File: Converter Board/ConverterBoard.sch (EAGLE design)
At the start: 40 parts

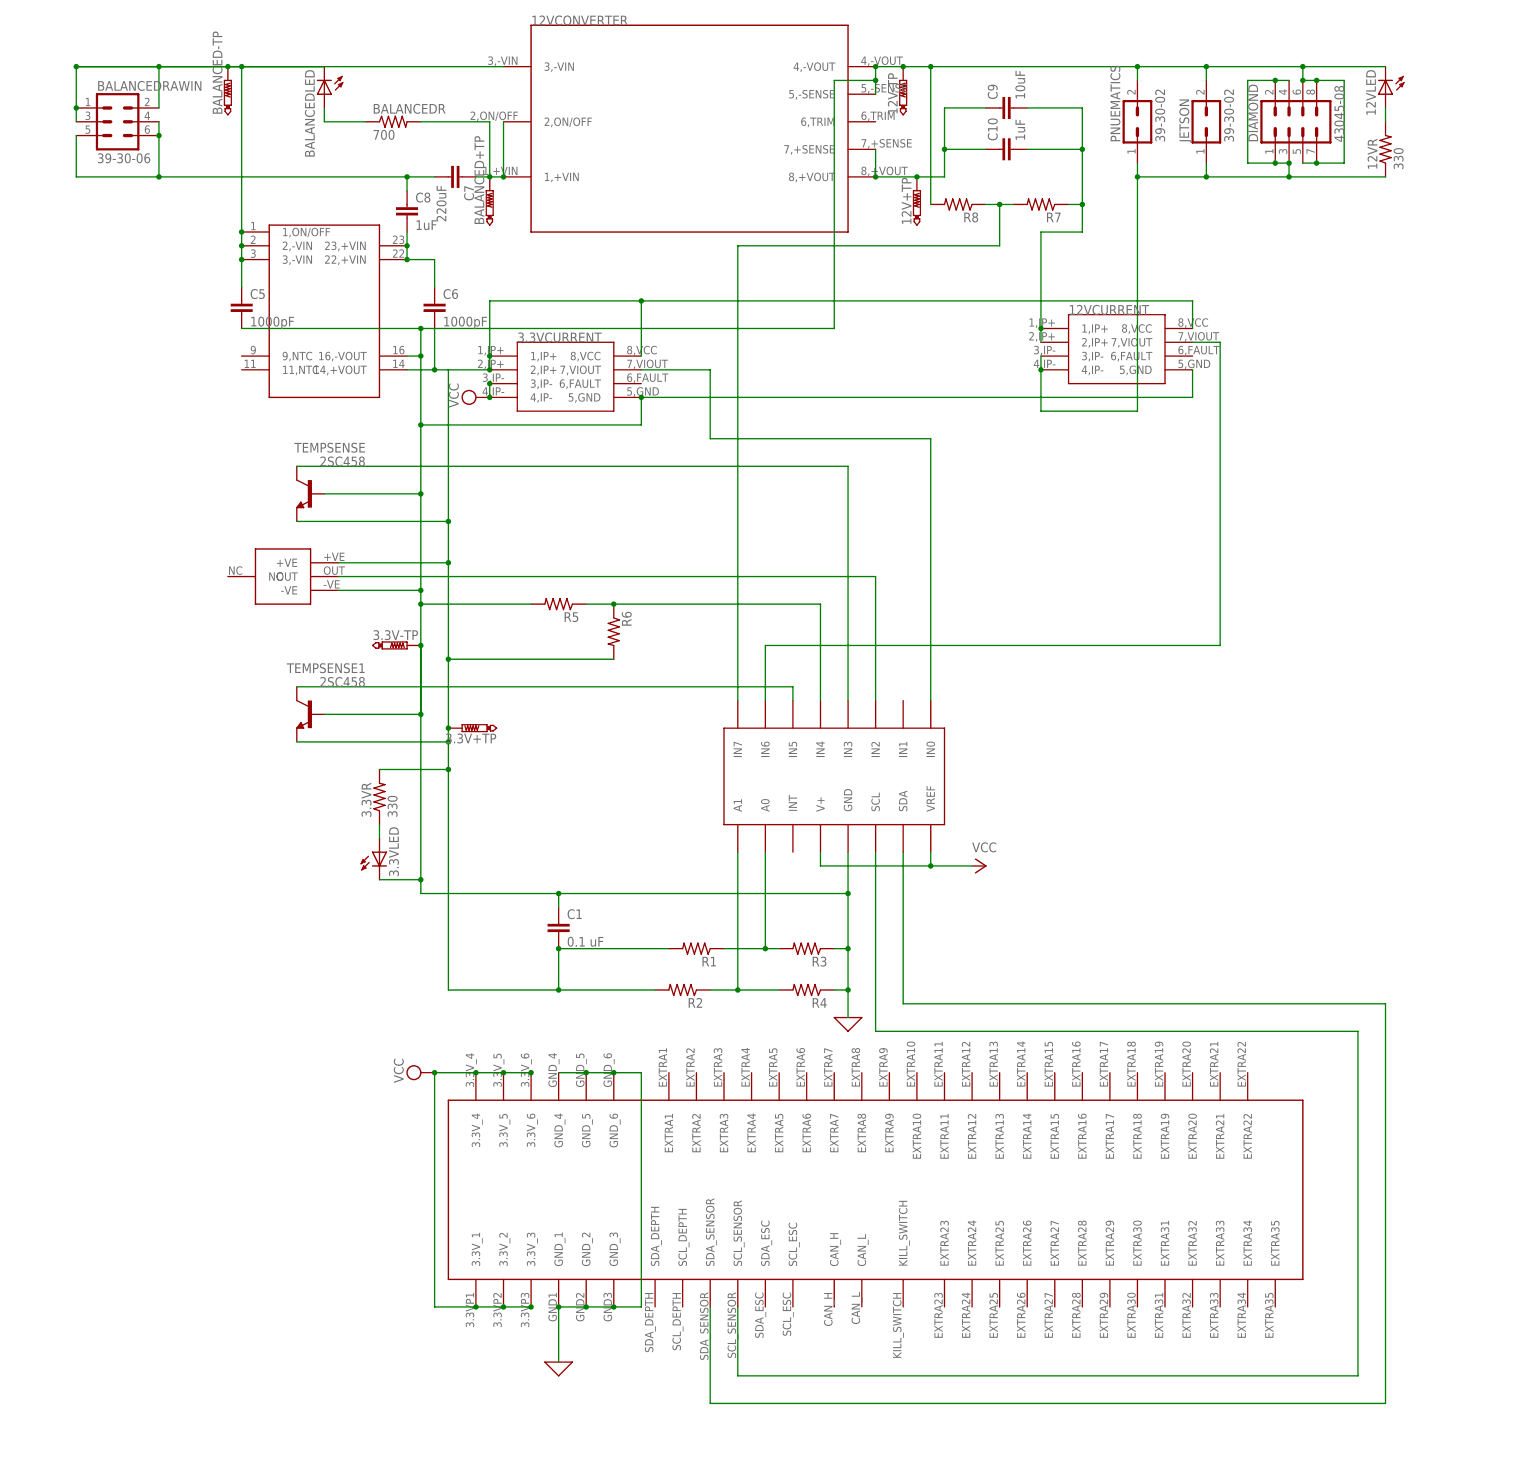
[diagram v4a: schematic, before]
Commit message: Finished Rev 3 of converter board
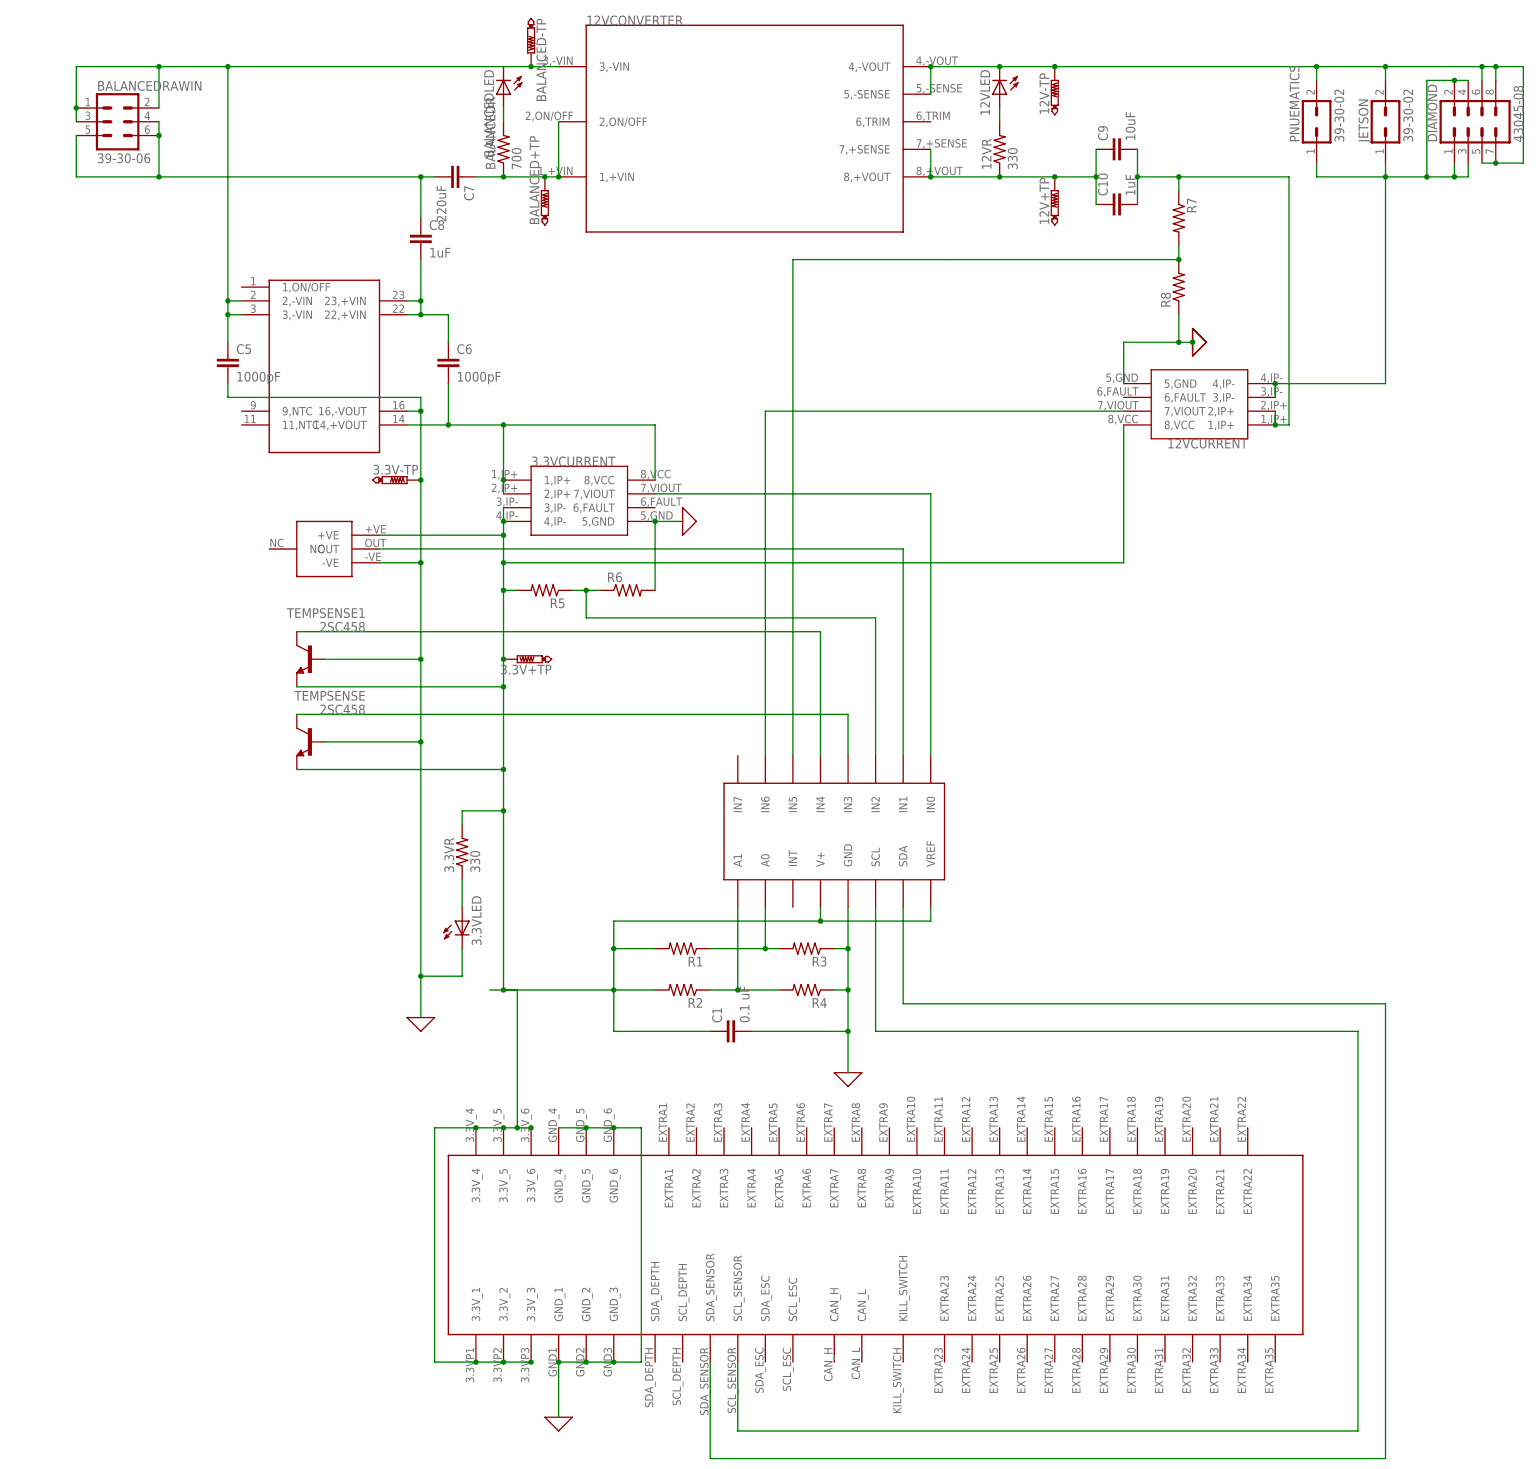
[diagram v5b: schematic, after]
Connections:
- net 12IDATA renamed 12VCURRENTDATA
- net 3.3IDATA renamed 3.3VCURRENTDATA
- net 3.3VC renamed 3.3VCONVIN
- removed net 12V+: 12V+TP.TP, 12VCONVERTER.7,+SENSE, 12VCONVERTER.8,+VOUT, C10.1, C9.1
- removed net 12VCIN: 12VCONVERTER.1,+VIN, 12VCONVERTER.2,ON/OFF, 12VCURRENT.1,IP+, 12VCURRENT.2,IP+, BALANCED+TP.TP, BALANCEDR.2, C10.2, C7.1, C9.2, R7.1
- removed net 12VCOUT: 12VCURRENT.3,IP-, 12VCURRENT.4,IP-, 12VR.1, DIAMOND.1, DIAMOND.2, DIAMOND.3, DIAMOND.4, JETSON.1, PNUEMATICS.1
- removed net 12VDATA: R7.2, R8.1, U$8.IN7
- removed net 3.3V+: 12VCURRENT.8,VCC, 3.3V+TP.TP, 3.3VCURRENT.1,IP+, 3.3VCURRENT.2,IP+, 3.3VCURRENT.8,VCC, 3.3VR.2, C1.2, C6.2, R1.2, R2.2, R6.2, TEMPSENSE.E, TEMPSENSE1.E, U$2.14,+VOUT, U$6.+VE
- removed net GND: 12V-TP.TP, 12VCONVERTER.4,-VOUT, 12VCONVERTER.5,-SENSE, 12VCURRENT.5,GND, 12VLED.C, 3.3V-TP.TP, 3.3VCURRENT.5,GND, 3.3VLED.C, C1.1, C5.2, DIAMOND.5, DIAMOND.6, DIAMOND.7, DIAMOND.8, JETSON.2, PNUEMATICS.2, R3.1, R4.1, R5.2, R8.2, TEMPSENSE.B, TEMPSENSE1.B, U$2.16,-VOUT, U$6.-VE, U$8.GND
- removed net VCC: 3.3VCURRENT.3,IP-, 3.3VCURRENT.4,IP-, U$3.3.3V_1, U$3.3.3V_2, U$3.3.3V_3, U$3.3.3V_4, U$3.3.3V_5, U$3.3.3V_6, U$8.V+, U$8.VREF
- new net 12VCONV+: 12V+TP.TP, 12VCONVERTER.7,+SENSE, 12VCONVERTER.8,+VOUT, 12VR.1, C10.1, C9.1
- new net 12VCONVIN: 12VCONVERTER.1,+VIN, 12VCONVERTER.2,ON/OFF, BALANCED+TP.TP, BALANCEDR.1, C7.1
- new net 12VCURRENTIN: 12VCURRENT.1,IP+, 12VCURRENT.2,IP+, C10.2, C9.2, R7.1
- new net 12VCURRENTOUT: 12VCURRENT.3,IP-, 12VCURRENT.4,IP-, DIAMOND.1, DIAMOND.2, DIAMOND.3, DIAMOND.4, JETSON.1, PNUEMATICS.1
- new net 12VDIV: R7.2, R8.2, U$8.IN5
- new net 3.3VCONVOUT: 3.3VCURRENT.1,IP+, 3.3VCURRENT.2,IP+, 3.3VCURRENT.8,VCC, C6.2, U$2.14,+VOUT
- new net 3.3VCURRENTOUT: 12VCURRENT.8,VCC, 3.3V+TP.TP, 3.3VCURRENT.3,IP-, 3.3VCURRENT.4,IP-, 3.3VR.2, C1.1, R1.2, R2.2, R5.2, TEMPSENSE.E, TEMPSENSE1.E, U$3.3.3V_1, U$3.3.3V_2, U$3.3.3V_3, U$3.3.3V_4, U$3.3.3V_5, U$3.3.3V_6, U$6.+VE, U$8.V+, U$8.VREF
- new net CMGND: 12V-TP.TP, 12VCONVERTER.4,-VOUT, 12VCONVERTER.5,-SENSE, 12VCURRENT.5,GND, 12VLED.C, 3.3V-TP.TP, 3.3VCURRENT.5,GND, 3.3VLED.C, C1.2, C5.2, DIAMOND.5, DIAMOND.6, DIAMOND.7, DIAMOND.8, JETSON.2, PNUEMATICS.2, R3.1, R4.1, R6.2, R8.1, TEMPSENSE.B, TEMPSENSE1.B, U$2.16,-VOUT, U$6.-VE, U$8.GND
- net 3.3VDATA: now also U$8.IN2; no longer U$8.IN4
- net BALANCEDGND: no longer U$2.1,ON/OFF
- net BALANCEDLED: now also BALANCEDR.2; no longer BALANCEDR.1
- net HUMIDITYDATA: now also U$8.IN1; no longer U$8.IN2
- net TEMP1DATA: now also U$8.IN4; no longer U$8.IN5
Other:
- moved on the sheet: 12V+TP, 12V-TP, 12VCONVERTER, 12VCURRENT, 12VLED, 12VR, 3.3V+TP, 3.3V-TP, 3.3VCURRENT, 3.3VLED, 3.3VR, BALANCED+TP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

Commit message: Finished rev3 of board, made gerber files
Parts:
- removed C1: 0.1 uF, resistor:C-EU025-024X044
- removed C10, C8: 1uF, resistor:C-EU025-024X044
- removed C6: 1000pF, resistor:C-EU025-024X044
- removed C7: 220uF, resistor:C-EU025-024X044
- removed C9: 10uF, resistor:C-EU025-024X044
- added C11, C14: 1uF, capacitor-wima:C5/3
- added C12: 220uF, capacitor-wima:C5/3
- added C13: 10uF, capacitor-wima:C5/3
- added C3, C4: 1000pF, capacitor-wima:C5/3
- added SCL, SDA: TPPAD1-20, testpad:TPPAD1-20
- C5: value 1000pF -> 0.1uF; device resistor:C-EU025-024X044 -> capacitor-wima:C2.5/2
- renumbered U$8 to ADC
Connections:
- removed net 3.3VGND: U$3.GND_1, U$3.GND_2, U$3.GND_3, U$3.GND_4, U$3.GND_5, U$3.GND_6
- net 12VCONV+: now also C13.1, C14.1; no longer C10.1, C9.1
- net 12VCONVIN: now also C12.2; no longer C7.1
- net 12VCURRENTIN: now also C13.2, C14.2; no longer C10.2, C9.2
- net 3.3VCONVIN: now also C11.2, C3.1; no longer C6.1, C8.2
- net 3.3VCONVOUT: now also C3.2; no longer C6.2
- net 3.3VCURRENTOUT: now also C5.2; no longer C1.1
- net BALANCED+: now also C11.1, C12.1; no longer C7.2, C8.1
- net BALANCEDGND: now also C4.1; no longer C5.1
- net CMGND: now also C4.2, C5.1, U$3.GND_1, U$3.GND_2, U$3.GND_3, U$3.GND_4, U$3.GND_5, U$3.GND_6; no longer C1.2, C5.2
- net SCL: now also SCL.TP
- net SDA: now also SDA.TP
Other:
- moved on the sheet: C5

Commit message: Revamped Converter Board
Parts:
- added 12V, 3.3V: 39-30-02, con-molex-mini-fit:39-30-02
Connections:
- removed net 12VCONVIN: 12VCONVERTER.1,+VIN, 12VCONVERTER.2,ON/OFF, BALANCED+TP.TP, BALANCEDR.1, C12.2
- removed net 12VCURRENTIN: 12VCURRENT.1,IP+, 12VCURRENT.2,IP+, C13.2, C14.2, R7.1
- net 12VCONV+: now also 12VCURRENT.1,IP+, 12VCURRENT.2,IP+, R7.1
- net 12VCURRENTOUT: now also 12V.1
- net 3.3VCURRENTOUT: now also 3.3V.1
- net BALANCED+: now also 12VCONVERTER.1,+VIN, 12VCONVERTER.2,ON/OFF, BALANCED+TP.TP, BALANCEDR.1
- net BALANCEDGND: now also C12.2
- net CMGND: now also 12V.2, 3.3V.2, C13.2, C14.2
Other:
- moved on the sheet: C12, C13, C14
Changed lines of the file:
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@@
 <?xml version="1.0" encoding="utf-8"?>
 <!DOCTYPE eagle SYSTEM "eagle.dtd">
-<eagle version="8.6.0">
+<eagle version="8.3.2">
 <drawing>
 <settings>
@@
 <part name="SDA" library="testpad" library_urn="urn:adsk.eagle:library:385" deviceset="TP" device="PAD1-20" package3d_urn="urn:adsk.eagle:package:27950/1"/>
 <part name="SCL" library="testpad" library_urn="urn:adsk.eagle:library:385" deviceset="TP" device="PAD1-20" package3d_urn="urn:adsk.eagle:package:27950/1"/>
+<part name="12V" library="con-molex-mini-fit" deviceset="39-30-?02?" device=""/>
+<part name="3.3V" library="con-molex-mini-fit" deviceset="39-30-?02?" device=""/>
 </parts>
 <sheets>
@@
 <instance part="C4" gate="G$1" x="-45.72" y="35.56"/>
 <instance part="C11" gate="G$1" x="-10.16" y="58.42"/>
-<instance part="C12" gate="G$1" x="-5.08" y="68.58" rot="R90"/>
-<instance part="C13" gate="G$1" x="116.84" y="73.66" rot="R90"/>
-<instance part="C14" gate="G$1" x="116.84" y="63.5" rot="R90"/>
+<instance part="C12" gate="G$1" x="-27.94" y="78.74" rot="R180"/>
+<instance part="C13" gate="G$1" x="124.46" y="78.74" rot="R180"/>
+<instance part="C14" gate="G$1" x="114.3" y="78.74" rot="R180"/>
 <instance part="C5" gate="G$1" x="48.26" y="-88.9" rot="R270"/>
 <instance part="SDA" gate="G$1" x="104.14" y="-81.28"/>
 <instance part="SCL" gate="G$1" x="124.46" y="-91.44" rot="R180"/>
+<instance part="12V" gate="G$1" x="144.78" y="78.74" rot="R90"/>
+<instance part="3.3V" gate="G$1" x="17.78" y="-93.98"/>
 </instances>
 <busses>
@@
 <pinref part="BALANCEDRAWIN" gate="G$1" pin="5"/>
 <wire x1="-73.66" y1="76.2" x2="-73.66" y2="68.58" width="0.1524" layer="91"/>
-<wire x1="-58.42" y1="68.58" x2="-10.16" y2="68.58" width="0.1524" layer="91"/>
+<wire x1="-58.42" y1="68.58" x2="-27.94" y2="68.58" width="0.1524" layer="91"/>
 <junction x="-58.42" y="68.58"/>
-<wire x1="-10.16" y1="68.58" x2="-7.62" y2="68.58" width="0.1524" layer="91"/>
+<wire x1="-27.94" y1="68.58" x2="-10.16" y2="68.58" width="0.1524" layer="91"/>
 <wire x1="-10.16" y1="60.96" x2="-10.16" y2="68.58" width="0.1524" layer="91"/>
+<pinref part="C11" gate="G$1" pin="1"/>
 <junction x="-10.16" y="68.58"/>
-<pinref part="C11" gate="G$1" pin="1"/>
+<pinref part="BALANCEDR" gate="G$1" pin="1"/>
+<pinref part="12VCONVERTER" gate="G$1" pin="1,+VIN"/>
+<wire x1="5.08" y1="68.58" x2="12.7" y2="68.58" width="0.1524" layer="91"/>
+<pinref part="12VCONVERTER" gate="G$1" pin="2,ON/OFF"/>
+<wire x1="12.7" y1="68.58" x2="15.24" y2="68.58" width="0.1524" layer="91"/>
+<wire x1="15.24" y1="78.74" x2="15.24" y2="68.58" width="0.1524" layer="91"/>
+<junction x="15.24" y="68.58"/>
+<pinref part="BALANCED+TP" gate="G$1" pin="TP"/>
+<junction x="12.7" y="68.58"/>
+<wire x1="-10.16" y1="68.58" x2="5.08" y2="68.58" width="0.1524" layer="91"/>
+<junction x="5.08" y="68.58"/>
 <pinref part="C12" gate="G$1" pin="1"/>
+<wire x1="-27.94" y1="76.2" x2="-27.94" y2="68.58" width="0.1524" layer="91"/>
+<junction x="-27.94" y="68.58"/>
 </segment>
 </net>
@@
 <wire x1="-7.62" y1="-106.68" x2="-7.62" y2="-149.86" width="0.1524" layer="91"/>
 <pinref part="U$3" gate="G$1" pin="3.3V_6"/>
-<junction x="10.16" y="-106.68"/>
 <pinref part="U$3" gate="G$1" pin="3.3V_5"/>
 <junction x="5.08" y="-106.68"/>
@@
 <pinref part="C5" gate="G$1" pin="2"/>
 <junction x="43.18" y="-88.9"/>
+<pinref part="3.3V" gate="G$1" pin="1"/>
+<wire x1="10.16" y1="-93.98" x2="10.16" y2="-106.68" width="0.1524" layer="91"/>
+<junction x="10.16" y="-106.68"/>
 </segment>
 </net>
@@
 <wire x1="180.34" y1="71.12" x2="180.34" y2="68.58" width="0.1524" layer="91"/>
 <junction x="180.34" y="68.58"/>
+<pinref part="12V" gate="G$1" pin="1"/>
+<wire x1="144.78" y1="71.12" x2="154.94" y2="71.12" width="0.1524" layer="91"/>
+<junction x="154.94" y="71.12"/>
 </segment>
 </net>
@@
 <junction x="96.52" y="88.9"/>
 <pinref part="12V-TP" gate="G$1" pin="TP"/>
-<wire x1="106.68" y1="88.9" x2="154.94" y2="88.9" width="0.1524" layer="91"/>
+<wire x1="106.68" y1="88.9" x2="114.3" y2="88.9" width="0.1524" layer="91"/>
 <junction x="106.68" y="88.9"/>
 <pinref part="DIAMOND" gate="G$1" pin="6"/>
+<wire x1="114.3" y1="88.9" x2="124.46" y2="88.9" width="0.1524" layer="91"/>
+<wire x1="124.46" y1="88.9" x2="144.78" y2="88.9" width="0.1524" layer="91"/>
+<wire x1="144.78" y1="88.9" x2="154.94" y2="88.9" width="0.1524" layer="91"/>
 <wire x1="185.42" y1="86.36" x2="185.42" y2="88.9" width="0.1524" layer="91"/>
 <junction x="185.42" y="88.9"/>
@@
 <wire x1="83.82" y1="83.82" x2="83.82" y2="88.9" width="0.1524" layer="91"/>
 <junction x="83.82" y="88.9"/>
+<pinref part="12V" gate="G$1" pin="2"/>
+<wire x1="144.78" y1="86.36" x2="144.78" y2="88.9" width="0.1524" layer="91"/>
+<junction x="144.78" y="88.9"/>
+<pinref part="C14" gate="G$1" pin="2"/>
+<wire x1="114.3" y1="83.82" x2="114.3" y2="88.9" width="0.1524" layer="91"/>
+<junction x="114.3" y="88.9"/>
+<pinref part="C13" gate="G$1" pin="2"/>
+<wire x1="124.46" y1="88.9" x2="124.46" y2="83.82" width="0.1524" layer="91"/>
+<junction x="124.46" y="88.9"/>
 </segment>
 <segment>
@@
 <wire x1="30.48" y1="-106.68" x2="30.48" y2="-149.86" width="0.1524" layer="91"/>
 <pinref part="3.3VGND" gate="G$1" pin="0"/>
+<pinref part="3.3V" gate="G$1" pin="2"/>
+<wire x1="25.4" y1="-93.98" x2="25.4" y2="-106.68" width="0.1524" layer="91"/>
 </segment>
 </net>
@@
 <wire x1="96.52" y1="68.58" x2="106.68" y2="68.58" width="0.1524" layer="91"/>
 <wire x1="106.68" y1="68.58" x2="114.3" y2="68.58" width="0.1524" layer="91"/>
-<wire x1="114.3" y1="68.58" x2="114.3" y2="73.66" width="0.1524" layer="91"/>
-<wire x1="114.3" y1="68.58" x2="114.3" y2="63.5" width="0.1524" layer="91"/>
-<junction x="114.3" y="68.58"/>
 <pinref part="12VCONVERTER" gate="G$1" pin="8,+VOUT"/>
 <pinref part="12VR" gate="G$1" pin="1"/>
@@
 <wire x1="83.82" y1="73.66" x2="83.82" y2="68.58" width="0.1524" layer="91"/>
 <junction x="83.82" y="68.58"/>
-<pinref part="C13" gate="G$1" pin="1"/>
 <pinref part="C14" gate="G$1" pin="1"/>
-</segment>
-</net>
-<net name="12VCURRENTIN" class="0">
-<segment>
-<wire x1="121.92" y1="73.66" x2="121.92" y2="68.58" width="0.1524" layer="91"/>
-<wire x1="121.92" y1="68.58" x2="121.92" y2="63.5" width="0.1524" layer="91"/>
-<wire x1="121.92" y1="68.58" x2="129.54" y2="68.58" width="0.1524" layer="91"/>
-<junction x="121.92" y="68.58"/>
+<wire x1="114.3" y1="76.2" x2="114.3" y2="68.58" width="0.1524" layer="91"/>
+<wire x1="114.3" y1="68.58" x2="121.92" y2="68.58" width="0.1524" layer="91"/>
+<junction x="114.3" y="68.58"/>
+<wire x1="121.92" y1="68.58" x2="124.46" y2="68.58" width="0.1524" layer="91"/>
 <pinref part="R7" gate="G$1" pin="1"/>
+<wire x1="124.46" y1="68.58" x2="129.54" y2="68.58" width="0.1524" layer="91"/>
 <wire x1="129.54" y1="68.58" x2="129.54" y2="66.04" width="0.1524" layer="91"/>
 <wire x1="129.54" y1="68.58" x2="149.86" y2="68.58" width="0.1524" layer="91"/>
@@
 <wire x1="149.86" y1="22.86" x2="147.32" y2="22.86" width="0.1524" layer="91"/>
 <junction x="147.32" y="22.86"/>
-<pinref part="C13" gate="G$1" pin="2"/>
-<pinref part="C14" gate="G$1" pin="2"/>
+<pinref part="C13" gate="G$1" pin="1"/>
+<wire x1="124.46" y1="76.2" x2="124.46" y2="68.58" width="0.1524" layer="91"/>
+<junction x="124.46" y="68.58"/>
+<junction x="121.92" y="68.58"/>
 </segment>
 </net>
@@
 <pinref part="12VLED" gate="G$1" pin="A"/>
 <wire x1="96.52" y1="78.74" x2="96.52" y2="81.28" width="0.1524" layer="91"/>
-</segment>
-</net>
-<net name="12VCONVIN" class="0">
-<segment>
-<pinref part="BALANCEDR" gate="G$1" pin="1"/>
-<wire x1="0" y1="68.58" x2="5.08" y2="68.58" width="0.1524" layer="91"/>
-<pinref part="12VCONVERTER" gate="G$1" pin="1,+VIN"/>
-<wire x1="5.08" y1="68.58" x2="12.7" y2="68.58" width="0.1524" layer="91"/>
-<junction x="5.08" y="68.58"/>
-<pinref part="12VCONVERTER" gate="G$1" pin="2,ON/OFF"/>
-<wire x1="12.7" y1="68.58" x2="15.24" y2="68.58" width="0.1524" layer="91"/>
-<wire x1="15.24" y1="78.74" x2="15.24" y2="68.58" width="0.1524" layer="91"/>
-<junction x="15.24" y="68.58"/>
-<pinref part="BALANCED+TP" gate="G$1" pin="TP"/>
-<junction x="12.7" y="68.58"/>
-<pinref part="C12" gate="G$1" pin="2"/>
 </segment>
 </net>
@@
 <wire x1="-58.42" y1="88.9" x2="-45.72" y2="88.9" width="0.1524" layer="91"/>
 <junction x="-58.42" y="88.9"/>
-<wire x1="-45.72" y1="88.9" x2="5.08" y2="88.9" width="0.1524" layer="91"/>
+<wire x1="-45.72" y1="88.9" x2="-27.94" y2="88.9" width="0.1524" layer="91"/>
+<wire x1="-27.94" y1="88.9" x2="5.08" y2="88.9" width="0.1524" layer="91"/>
 <wire x1="-45.72" y1="45.72" x2="-45.72" y2="88.9" width="0.1524" layer="91"/>
 <junction x="-45.72" y="45.72"/>
@@
 <junction x="10.16" y="88.9"/>
 <pinref part="C4" gate="G$1" pin="1"/>
-</segment>
-</net>
+<pinref part="C12" gate="G$1" pin="2"/>
+<wire x1="-27.94" y1="83.82" x2="-27.94" y2="88.9" width="0.1524" layer="91"/>
+<junction x="-27.94" y="88.9"/>
+</segment>
+</net>
